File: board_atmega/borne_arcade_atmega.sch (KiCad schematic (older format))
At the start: 43 parts, among them P1 MUSB, P2 CONN_15, P3 CONN_15, U1 ATMEGA32U4, X1 QUARTZ_CMS_4

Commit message: Adding page information (licence, version, author) Adding logos
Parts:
- added G1: LOGO, symbol LOGO
- added G2: LOGO_FOL, symbol LOGO_FOL
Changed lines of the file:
@@
 LIBS:serigraphie
 LIBS:device
+LIBS:serigraphie_fol
 LIBS:borne_arcade_atmega-cache
 EELAYER 27 0
@@
 encoding utf-8
 Sheet 1 1
-Title ""
-Date "7 jul 2014"
-Rev ""
-Comp ""
-Comment1 ""
-Comment2 ""
+Title "Borne Arcade FOL ATMega"
+Date "8 jul 2014"
+Rev "0.1"
+Comp "Fabrique d'Objets Libres - Techno-Innov"
+Comment1 "Licence : CC-By-SA"
+Comment2 "Author : Nathael Pajani - nathael.pajani@techno-innov.fr"
 Comment3 ""
 Comment4 ""
@@
 $EndComp
 $Comp
-L DGND #PWR01
+L DGND #PWR1
 U 1 1 53BB113B
 P 1150 4350
-F 0 "#PWR01" H 1150 4350 40  0001 C CNN
+F 0 "#PWR1" H 1150 4350 40  0001 C CNN
 F 1 "DGND" H 1150 4250 40  0000 C CNN
 F 2 "" H 1150 4350 60  0000 C CNN
@@
 $EndComp
 $Comp
-L DGND #PWR02
+L DGND #PWR3
 U 1 1 53BB11AE
 P 1650 4800
-F 0 "#PWR02" H 1650 4800 40  0001 C CNN
+F 0 "#PWR3" H 1650 4800 40  0001 C CNN
 F 1 "DGND" H 1650 4700 40  0000 C CNN
 F 2 "" H 1650 4800 60  0000 C CNN
@@
 $EndComp
 $Comp
-L DGND #PWR03
+L DGND #PWR8
 U 1 1 53BB11C3
 P 2900 5300
-F 0 "#PWR03" H 2900 5300 40  0001 C CNN
+F 0 "#PWR8" H 2900 5300 40  0001 C CNN
 F 1 "DGND" H 2900 5200 40  0000 C CNN
 F 2 "" H 2900 5300 60  0000 C CNN
@@
 $EndComp
 $Comp
-L DGND #PWR04
+L DGND #PWR5
 U 1 1 53BB1554
 P 1900 5050
-F 0 "#PWR04" H 1900 5050 40  0001 C CNN
+F 0 "#PWR5" H 1900 5050 40  0001 C CNN
 F 1 "DGND" H 1900 4950 40  0000 C CNN
 F 2 "" H 1900 5050 60  0000 C CNN
@@
 $EndComp
 $Comp
-L DGND #PWR05
+L DGND #PWR7
 U 1 1 53BB155A
 P 2700 5050
-F 0 "#PWR05" H 2700 5050 40  0001 C CNN
+F 0 "#PWR7" H 2700 5050 40  0001 C CNN
 F 1 "DGND" H 2700 4950 40  0000 C CNN
 F 2 "" H 2700 5050 60  0000 C CNN
@@
 $EndComp
 $Comp
-L DGND #PWR06
+L DGND #PWR6
 U 1 1 53BB1560
 P 2300 4700
-F 0 "#PWR06" H 2300 4700 40  0001 C CNN
+F 0 "#PWR6" H 2300 4700 40  0001 C CNN
 F 1 "DGND" H 2300 4600 40  0000 C CNN
 F 2 "" H 2300 4700 60  0000 C CNN
@@
 $EndComp
 $Comp
-L DGND #PWR07
+L DGND #PWR2
 U 1 1 53BB1721
 P 1400 4650
-F 0 "#PWR07" H 1400 4650 40  0001 C CNN
+F 0 "#PWR2" H 1400 4650 40  0001 C CNN
 F 1 "DGND" H 1400 4550 40  0000 C CNN
 F 2 "" H 1400 4650 60  0000 C CNN
@@
 $EndComp
 $Comp
-L DGND #PWR08
+L DGND #PWR4
 U 1 1 53BB17E4
 P 1850 3100
-F 0 "#PWR08" H 1850 3100 40  0001 C CNN
+F 0 "#PWR4" H 1850 3100 40  0001 C CNN
 F 1 "DGND" H 1850 3000 40  0000 C CNN
 F 2 "" H 1850 3100 60  0000 C CNN
@@
 Connection ~ 10150 5350
 $Comp
-L DGND #PWR09
+L DGND #PWR9
 U 1 1 53BB6CB9
 P 10350 5650
-F 0 "#PWR09" H 10350 5650 40  0001 C CNN
+F 0 "#PWR9" H 10350 5650 40  0001 C CNN
 F 1 "DGND" H 10350 5550 40  0000 C CNN
 F 2 "" H 10350 5650 60  0000 C CNN
@@
 	10300 4050 10450 4050
 Connection ~ 10300 2350
+$Comp
+L LOGO G1
+U 1 1 53BBD2C0
+P 6650 7150
+F 0 "G1" H 6650 6927 60  0001 C CNN
+F 1 "LOGO" H 6650 7373 60  0001 C CNN
+F 2 "" H 6650 7150 60  0000 C CNN
+F 3 "" H 6650 7150 60  0000 C CNN
+	1    6650 7150
+	1    0    0    -1
+$EndComp
+$Comp
+L LOGO_FOL G2
+U 1 1 53BBD712
+P 6650 7550
+F 0 "G2" H 6650 7414 60  0001 C CNN
+F 1 "LOGO_FOL" H 6650 7686 60  0001 C CNN
+F 2 "" H 6650 7550 60  0000 C CNN
+F 3 "" H 6650 7550 60  0000 C CNN
+	1    6650 7550
+	1    0    0    -1
+$EndComp
 $EndSCHEMATC

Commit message: Layout and some modifications to ease layout
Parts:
- added H1, H2, H3: HOLE_3MM, ~, symbol HOLE_3MM
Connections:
- net +5V_USB: now reaches FB1.1, P1.1 (+V)
- net D-_USB: now reaches P1.2 (D-), R1.1
- net D+_USB: now reaches P1.3 (D+), R2.1
- net +5V: now reaches C1.1, C3.1, C5.1, C7.1, FB1.2, P2.1 (P1), P3.1 (P1), R10.1, R11.1, R12.1, R13.1, R14.1, R15.1, R16.1, R17.1, R18.1, R19.1, R20.1, R21.1, R22.1, R23.1, R24.1, R25.1, R26.1, R27.1, R28.1, R29.1, R3.1, R4.1, R5.1, R6.1, R7.1, R8.1, R9.1, U1.14 (VCC), U1.2 (UVCC), U1.24 (AVCC), U1.34 (VCC), U1.44 (AVCC), U1.7 (VBUS)
- net D-: now reaches R1.2, U1.3 (D-)
- net D+: now reaches R2.2, U1.4 (D+)
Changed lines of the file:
@@
 U 1 1 53BAF2FD
 P 700 3950
-F 0 "P1" H 700 4350 60  0000 C CNN
-F 1 "MUSB" H 750 3550 60  0000 C CNN
+F 0 "P1" H 800 3650 60  0000 C CNN
+F 1 "MUSB" H 600 4350 60  0000 C CNN
 F 2 "~" H 700 3950 60  0000 C CNN
 F 3 "~" H 700 3950 60  0000 C CNN
@@
 	1    0    0    -1
 $EndComp
+Text Label 1150 1500 2    60   ~ 0
++5V
+Text Label 1150 3600 2    60   ~ 0
++5V_USB
+$Comp
+L HOLE_3MM H1
+U 1 1 53BBEB05
+P 3050 6900
+F 0 "H1" H 3050 6750 60  0000 C CNN
+F 1 "HOLE_3MM" H 3050 7050 60  0000 C CNN
+F 2 "~" H 3050 6900 60  0000 C CNN
+F 3 "~" H 3050 6900 60  0000 C CNN
+	1    3050 6900
+	1    0    0    -1
+$EndComp
+$Comp
+L HOLE_3MM H2
+U 1 1 53BBEB12
+P 3750 6900
+F 0 "H2" H 3750 6750 60  0000 C CNN
+F 1 "HOLE_3MM" H 3750 7050 60  0000 C CNN
+F 2 "~" H 3750 6900 60  0000 C CNN
+F 3 "~" H 3750 6900 60  0000 C CNN
+	1    3750 6900
+	1    0    0    -1
+$EndComp
+$Comp
+L HOLE_3MM H3
+U 1 1 53BBEB18
+P 4500 6900
+F 0 "H3" H 4500 6750 60  0000 C CNN
+F 1 "HOLE_3MM" H 4500 7050 60  0000 C CNN
+F 2 "~" H 4500 6900 60  0000 C CNN
+F 3 "~" H 4500 6900 60  0000 C CNN
+	1    4500 6900
+	1    0    0    -1
+$EndComp
+Text Label 2650 3950 0    40   ~ 0
+D+
+Text Label 2650 3850 0    40   ~ 0
+D-
+Text Label 1100 3850 0    40   ~ 0
+D-_USB
+Text Label 1100 3950 0    40   ~ 0
+D+_USB
 $EndSCHEMATC

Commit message: First version produced
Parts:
- added G3: LOGO_OSHW, symbol LOGO_OSHW
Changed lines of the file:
@@
 LIBS:device
 LIBS:serigraphie_fol
+LIBS:oshw
 LIBS:borne_arcade_atmega-cache
 EELAYER 27 0
@@
 Sheet 1 1
 Title "Borne Arcade FOL ATMega"
-Date "8 jul 2014"
+Date "17 jul 2014"
 Rev "0.1"
 Comp "Fabrique d'Objets Libres - Techno-Innov"
@@
 $EndComp
 $Comp
-L DGND #PWR1
+L DGND #PWR01
 U 1 1 53BB113B
 P 1150 4350
-F 0 "#PWR1" H 1150 4350 40  0001 C CNN
+F 0 "#PWR01" H 1150 4350 40  0001 C CNN
 F 1 "DGND" H 1150 4250 40  0000 C CNN
 F 2 "" H 1150 4350 60  0000 C CNN
@@
 $EndComp
 $Comp
-L DGND #PWR3
+L DGND #PWR02
 U 1 1 53BB11AE
 P 1650 4800
-F 0 "#PWR3" H 1650 4800 40  0001 C CNN
+F 0 "#PWR02" H 1650 4800 40  0001 C CNN
 F 1 "DGND" H 1650 4700 40  0000 C CNN
 F 2 "" H 1650 4800 60  0000 C CNN
@@
 $EndComp
 $Comp
-L DGND #PWR8
+L DGND #PWR03
 U 1 1 53BB11C3
 P 2900 5300
-F 0 "#PWR8" H 2900 5300 40  0001 C CNN
+F 0 "#PWR03" H 2900 5300 40  0001 C CNN
 F 1 "DGND" H 2900 5200 40  0000 C CNN
 F 2 "" H 2900 5300 60  0000 C CNN
@@
 $EndComp
 $Comp
-L DGND #PWR5
+L DGND #PWR04
 U 1 1 53BB1554
 P 1900 5050
-F 0 "#PWR5" H 1900 5050 40  0001 C CNN
+F 0 "#PWR04" H 1900 5050 40  0001 C CNN
 F 1 "DGND" H 1900 4950 40  0000 C CNN
 F 2 "" H 1900 5050 60  0000 C CNN
@@
 $EndComp
 $Comp
-L DGND #PWR7
+L DGND #PWR05
 U 1 1 53BB155A
 P 2700 5050
-F 0 "#PWR7" H 2700 5050 40  0001 C CNN
+F 0 "#PWR05" H 2700 5050 40  0001 C CNN
 F 1 "DGND" H 2700 4950 40  0000 C CNN
 F 2 "" H 2700 5050 60  0000 C CNN
@@
 $EndComp
 $Comp
-L DGND #PWR6
+L DGND #PWR06
 U 1 1 53BB1560
 P 2300 4700
-F 0 "#PWR6" H 2300 4700 40  0001 C CNN
+F 0 "#PWR06" H 2300 4700 40  0001 C CNN
 F 1 "DGND" H 2300 4600 40  0000 C CNN
 F 2 "" H 2300 4700 60  0000 C CNN
@@
 $EndComp
 $Comp
-L DGND #PWR2
+L DGND #PWR07
 U 1 1 53BB1721
 P 1400 4650
-F 0 "#PWR2" H 1400 4650 40  0001 C CNN
+F 0 "#PWR07" H 1400 4650 40  0001 C CNN
 F 1 "DGND" H 1400 4550 40  0000 C CNN
 F 2 "" H 1400 4650 60  0000 C CNN
@@
 $EndComp
 $Comp
-L DGND #PWR4
+L DGND #PWR08
 U 1 1 53BB17E4
 P 1850 3100
-F 0 "#PWR4" H 1850 3100 40  0001 C CNN
+F 0 "#PWR08" H 1850 3100 40  0001 C CNN
 F 1 "DGND" H 1850 3000 40  0000 C CNN
 F 2 "" H 1850 3100 60  0000 C CNN
@@
 Connection ~ 10150 5350
 $Comp
-L DGND #PWR9
+L DGND #PWR09
 U 1 1 53BB6CB9
 P 10350 5650
-F 0 "#PWR9" H 10350 5650 40  0001 C CNN
+F 0 "#PWR09" H 10350 5650 40  0001 C CNN
 F 1 "DGND" H 10350 5550 40  0000 C CNN
 F 2 "" H 10350 5650 60  0000 C CNN
@@
 Text Label 1100 3950 0    40   ~ 0
 D+_USB
+$Comp
+L LOGO_OSHW G3
+U 1 1 53C7ED64
+P 6650 6750
+F 0 "G3" H 6650 6634 60  0001 C CNN
+F 1 "LOGO_OSHW" H 6650 6866 60  0001 C CNN
+F 2 "" H 6650 6750 60  0000 C CNN
+F 3 "" H 6650 6750 60  0000 C CNN
+	1    6650 6750
+	1    0    0    -1
+$EndComp
 $EndSCHEMATC

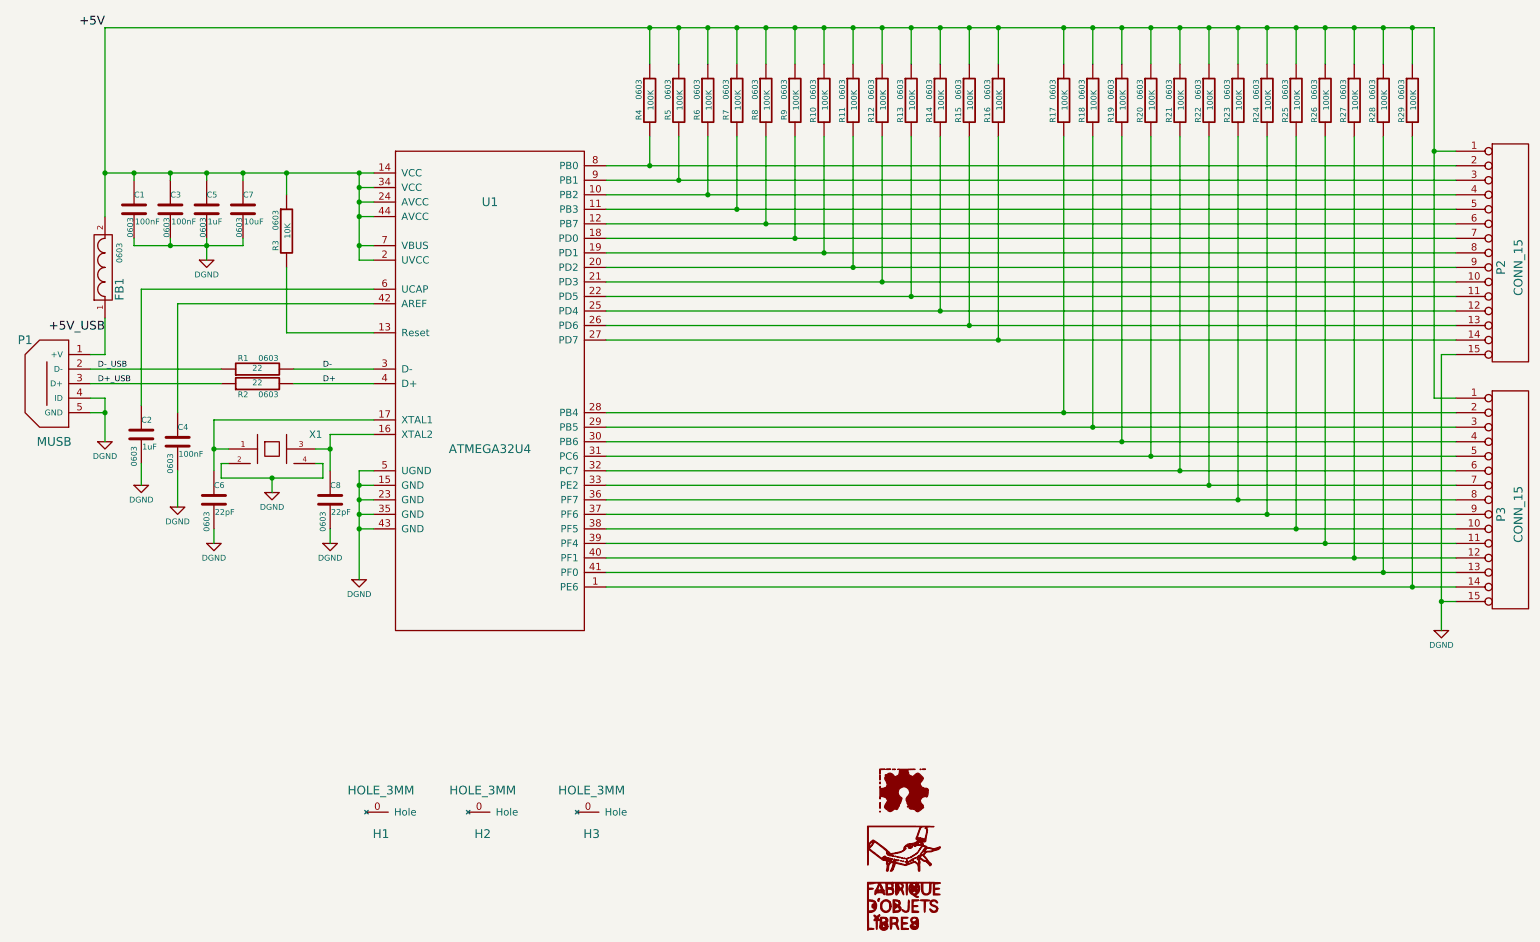
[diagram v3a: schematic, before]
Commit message: Nev revision v0.2 : - Adding the switches for reset and ISP mode selection - Addind reset pin - Changed USB connector to micro-USB (was mini-USB) - Adding power led - Using "arduino" names on top silkscreen and "Atmel" ones on bottom silkscreen
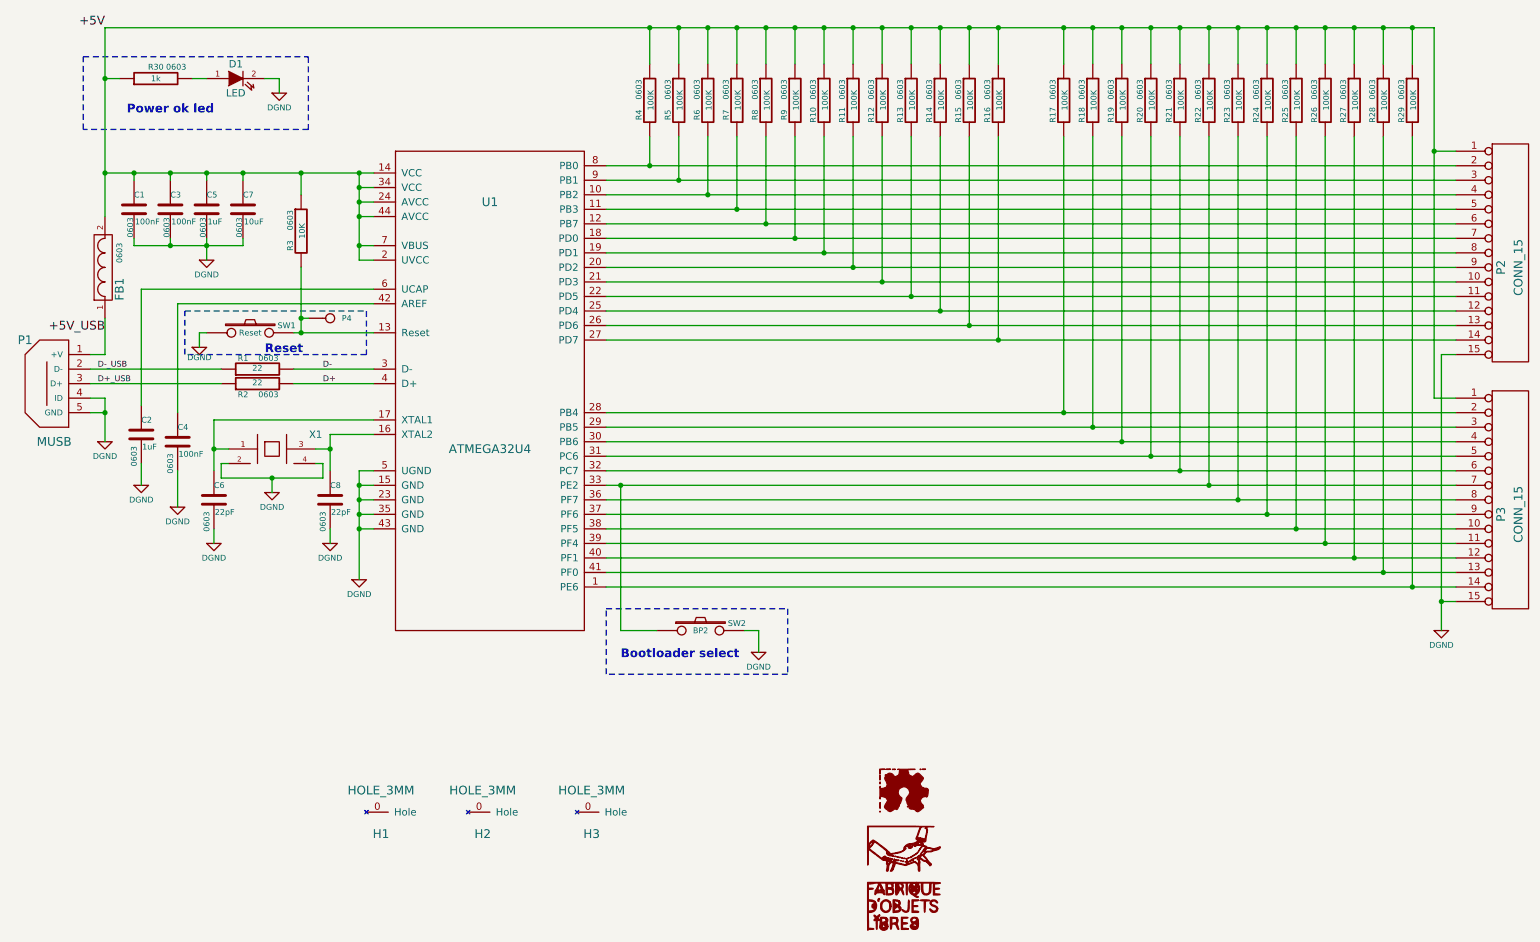
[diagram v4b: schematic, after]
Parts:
- added D1: LED, ~, symbol LED
- added P4: CONN_1, symbol CONN_1
- added R30: 1k, 0603, symbol R
- added SW1: Reset, symbol SW_PUSH
- added SW2: BP2, symbol SW_PUSH
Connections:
- net +5V: now also R30.1
- net DGND: now also D1.2 (K), SW1.1, SW2.2
- net at R3.2, U1.13 (Reset): now also P4.1, SW1.2
- net at P3.7 (P7), R22.2, U1.33 (PE2): now also SW2.1
- new net: D1.1 (A), R30.2
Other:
- note added: "Bootloader select"
- note added: "Power ok led"
- note added: "Reset"
- moved on the sheet: R3
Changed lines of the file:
@@
 LIBS:serigraphie_fol
 LIBS:oshw
+LIBS:conn
 LIBS:borne_arcade_atmega-cache
 EELAYER 27 0
@@
 Sheet 1 1
 Title "Borne Arcade FOL ATMega"
-Date "17 jul 2014"
-Rev "0.1"
+Date "21 sep 2014"
+Rev "0.2"
 Comp "Fabrique d'Objets Libres - Techno-Innov"
 Comment1 "Licence : CC-By-SA"
@@
 L R R3
 U 1 1 53BB175F
-P 2400 2900
-F 0 "R3" V 2325 2800 40  0000 C CNN
-F 1 "10K" V 2407 2901 40  0000 C CNN
-F 2 "0603" V 2325 2975 40  0000 C CNN
-F 3 "~" H 2400 2900 30  0000 C CNN
-	1    2400 2900
+P 2500 2900
+F 0 "R3" V 2425 2800 40  0000 C CNN
+F 1 "10K" V 2507 2901 40  0000 C CNN
+F 2 "0603" V 2425 2975 40  0000 C CNN
+F 3 "~" H 2500 2900 30  0000 C CNN
+	1    2500 2900
 	1    0    0    -1
 $EndComp
@@
 	1150 3750 1050 3750
 Wire Wire Line
-	1650 3400 3000 3400
-Wire Wire Line
 	1650 3400 1650 4150
 Wire Wire Line
@@
 Connection ~ 2700 4400
 Wire Wire Line
-	3000 3300 1400 3300
-Wire Wire Line
 	1400 3300 1400 4100
 Wire Wire Line
 	1400 4500 1400 4650
 Wire Wire Line
-	2400 2500 2400 2650
-Connection ~ 2400 2500
-Wire Wire Line
-	2400 3150 2400 3600
-Wire Wire Line
-	2400 3600 3000 3600
+	2500 2500 2500 2650
+Connection ~ 2500 2500
+Wire Wire Line
+	2500 3150 2500 3600
+Wire Wire Line
+	2450 3600 3000 3600
 Wire Wire Line
 	1350 2500 1350 2550
@@
 	1    0    0    -1
 $EndComp
+$Comp
+L SW_PUSH SW2
+U 1 1 541EA9E5
+P 5250 5650
+F 0 "SW2" H 5500 5700 40  0000 C CNN
+F 1 "BP2" H 5250 5650 40  0000 C CNN
+F 2 "" H 5250 5650 60  0001 C CNN
+F 3 "" H 5250 5650 60  0001 C CNN
+	1    5250 5650
+	1    0    0    -1
+$EndComp
+$Comp
+L R R30
+U 1 1 541EA9EB
+P 1500 1850
+F 0 "R30" V 1580 1850 40  0000 C CNN
+F 1 "1k" V 1500 1850 40  0000 C CNN
+F 2 "0603" V 1580 1710 40  0000 C CNN
+F 3 "" H 1500 1850 60  0001 C CNN
+	1    1500 1850
+	0    -1   -1   0
+$EndComp
+$Comp
+L DGND #PWR010
+U 1 1 541EA9F1
+P 1800 3700
+F 0 "#PWR010" H 1800 3700 40  0001 C CNN
+F 1 "DGND" H 1800 3630 40  0000 C CNN
+F 2 "" H 1800 3700 60  0001 C CNN
+F 3 "" H 1800 3700 60  0001 C CNN
+	1    1800 3700
+	1    0    0    -1
+$EndComp
+$Comp
+L SW_PUSH SW1
+U 1 1 541EA9FD
+P 2150 3600
+F 0 "SW1" H 2400 3650 40  0000 C CNN
+F 1 "Reset" H 2150 3600 40  0000 C CNN
+F 2 "" H 2150 3600 60  0001 C CNN
+F 3 "" H 2150 3600 60  0001 C CNN
+	1    2150 3600
+	1    0    0    -1
+$EndComp
+Connection ~ 2500 3600
+Wire Wire Line
+	1850 3600 1800 3600
+Wire Wire Line
+	1800 3600 1800 3700
+Wire Wire Line
+	4700 4650 4700 5650
+Wire Wire Line
+	4700 5650 4950 5650
+Connection ~ 4700 4650
+$Comp
+L DGND #PWR011
+U 1 1 541EAE38
+P 5650 5800
+F 0 "#PWR011" H 5650 5800 40  0001 C CNN
+F 1 "DGND" H 5650 5700 40  0000 C CNN
+F 2 "" H 5650 5800 60  0000 C CNN
+F 3 "" H 5650 5800 60  0000 C CNN
+	1    5650 5800
+	1    0    0    -1
+$EndComp
+Wire Wire Line
+	5550 5650 5650 5650
+Wire Wire Line
+	5650 5650 5650 5800
+$Comp
+L LED D1
+U 1 1 541EB041
+P 2050 1850
+F 0 "D1" H 2050 1950 50  0000 C CNN
+F 1 "LED" H 2050 1750 50  0000 C CNN
+F 2 "~" H 2050 1850 60  0000 C CNN
+F 3 "~" H 2050 1850 60  0000 C CNN
+	1    2050 1850
+	1    0    0    -1
+$EndComp
+$Comp
+L DGND #PWR012
+U 1 1 541EB04E
+P 2350 1950
+F 0 "#PWR012" H 2350 1950 40  0001 C CNN
+F 1 "DGND" H 2350 1850 40  0000 C CNN
+F 2 "" H 2350 1950 60  0000 C CNN
+F 3 "" H 2350 1950 60  0000 C CNN
+	1    2350 1950
+	1    0    0    -1
+$EndComp
+Wire Wire Line
+	1150 1850 1250 1850
+Connection ~ 1150 1850
+Wire Wire Line
+	1750 1850 1850 1850
+Wire Wire Line
+	2250 1850 2350 1850
+Wire Wire Line
+	2350 1850 2350 1950
+Wire Notes Line
+	1000 1700 2550 1700
+Wire Notes Line
+	2550 1700 2550 2200
+Wire Notes Line
+	2550 2200 1000 2200
+Wire Notes Line
+	1000 2200 1000 1700
+Text Notes 1300 2100 0    60   ~ 12
+Power ok led
+Text Notes 4700 5850 0    60   ~ 12
+Bootloader select
+Wire Notes Line
+	4600 5500 5850 5500
+Wire Notes Line
+	5850 5500 5850 5950
+Wire Notes Line
+	5850 5950 4600 5950
+Wire Notes Line
+	4600 5950 4600 5500
+$Comp
+L CONN_1 P4
+U 1 1 541EB4D4
+P 2700 3500
+F 0 "P4" H 2780 3500 40  0000 L CNN
+F 1 "CONN_1" H 2700 3555 30  0001 C CNN
+F 2 "" H 2700 3500 60  0000 C CNN
+F 3 "" H 2700 3500 60  0000 C CNN
+	1    2700 3500
+	1    0    0    -1
+$EndComp
+Wire Wire Line
+	2550 3500 2500 3500
+Connection ~ 2500 3500
+Wire Notes Line
+	1700 3450 2950 3450
+Wire Notes Line
+	2950 3450 2950 3750
+Wire Notes Line
+	2950 3750 1700 3750
+Wire Notes Line
+	1700 3750 1700 3450
+Text Notes 2250 3750 0    60   ~ 12
+Reset
+Wire Wire Line
+	1650 3400 3000 3400
+Wire Wire Line
+	1400 3300 3000 3300
 $EndSCHEMATC
